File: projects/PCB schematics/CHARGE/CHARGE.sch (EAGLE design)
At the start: 30 parts, among them IC2 78L08SMD, Q1 IRLZ44Z, Q2 IRLZ44Z

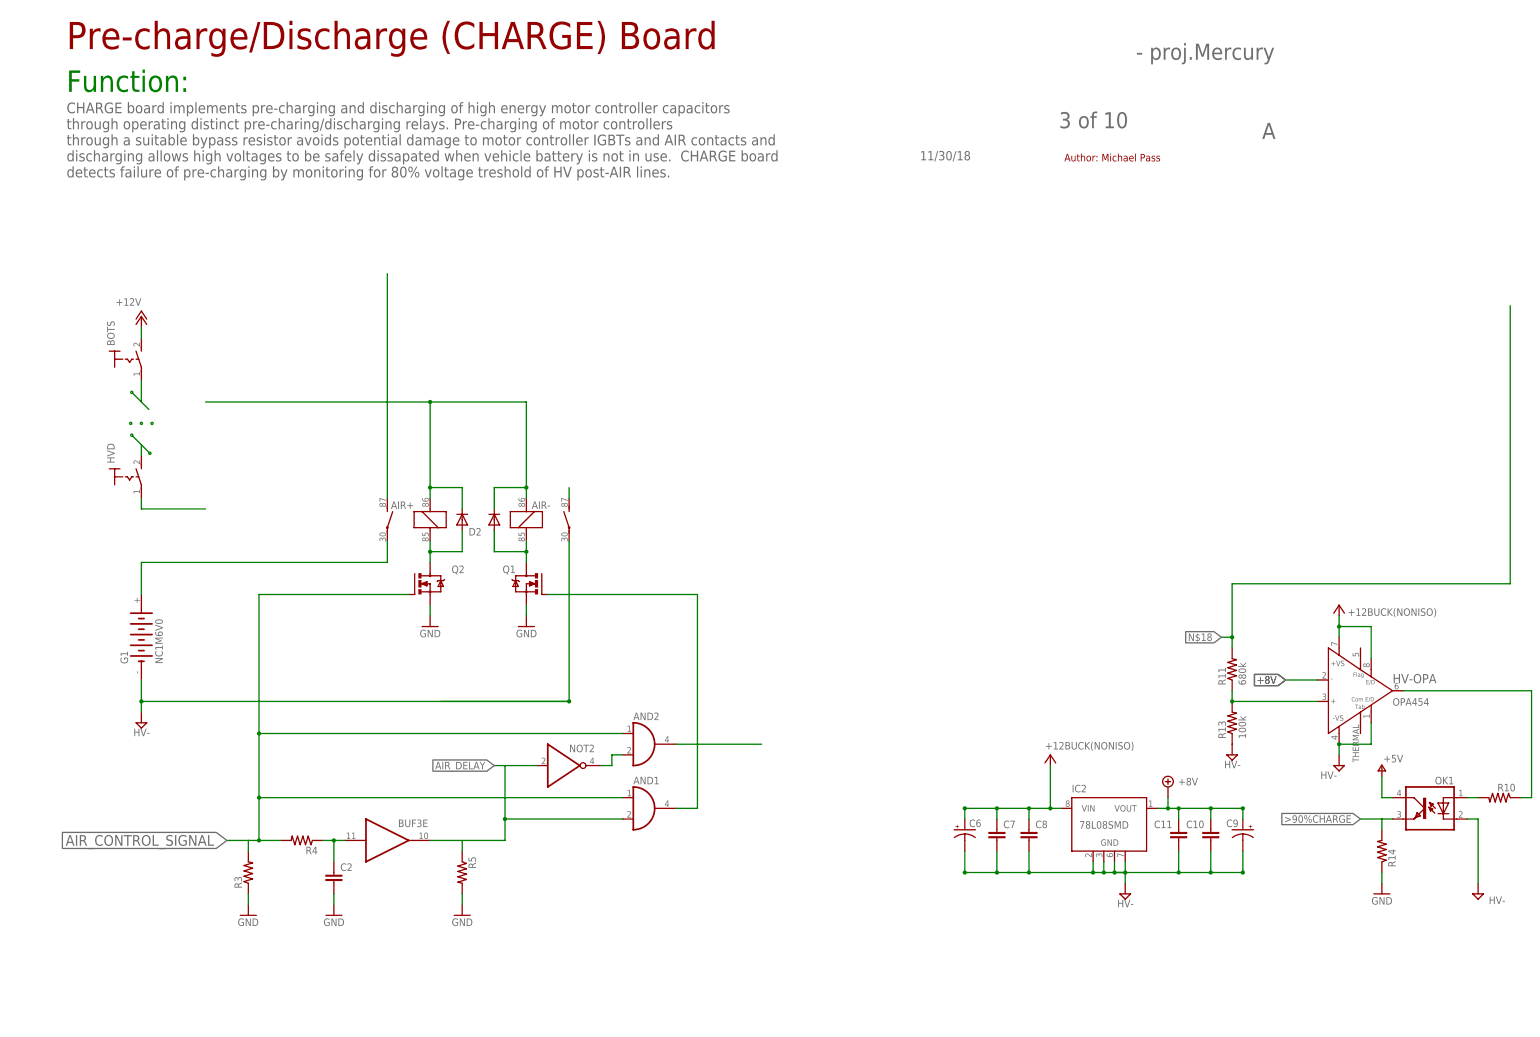
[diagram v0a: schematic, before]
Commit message: PROJ - Pulling in changes from mmp-CHARGE for ZEVA pre-charge
A library part was needed for ZEVA smart precharger  in order to play around with board placement. Very close approximation for footprint, with exact drill hole location achieved.

Amend - Incorrect stash attempt. Files copies over manually
from working mmp-CHARGE.
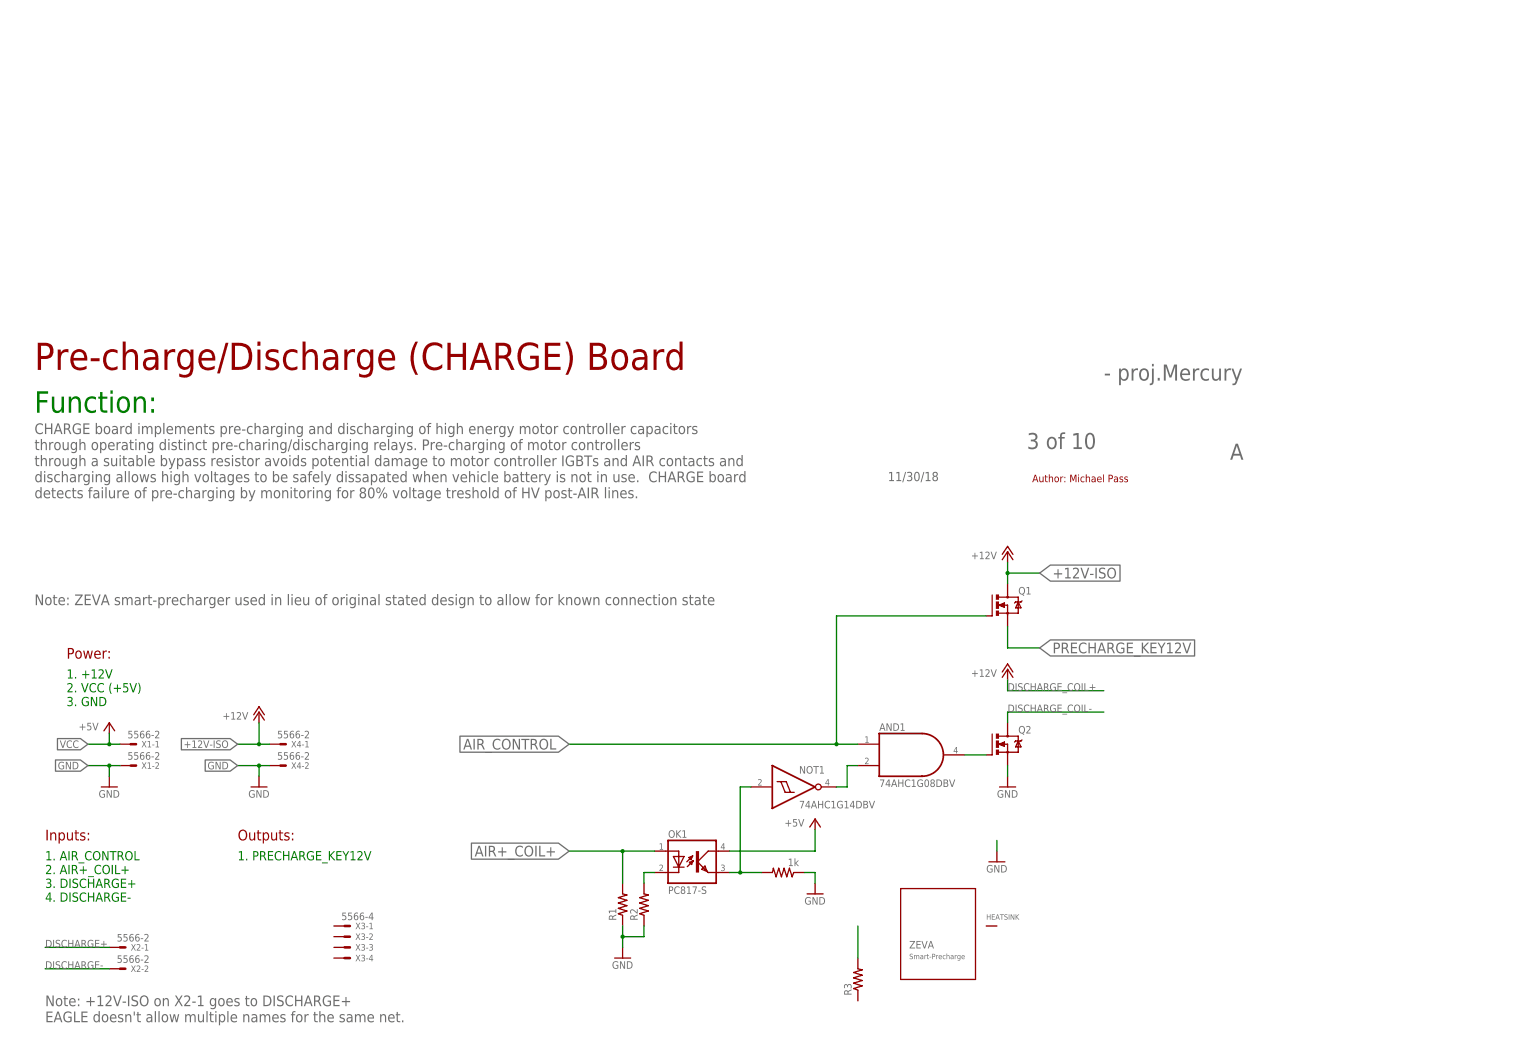
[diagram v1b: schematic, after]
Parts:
- removed AIR+, AIR-: CB1A-P-12V, relay:CB1A-P-12V
- removed AND2: 74AHCT1G08DCK, 74xx-little-de:74AHCT1G08DCK
- removed BOTS, HVD: (no value), switch:MS243
- removed BUF3: 7407D, 74xx-eu:7407D
- removed C10, C11, C7, C8: 0.1uF, rcl:C-EUC0805
- removed C2: (no value), rcl:C-EUC0805
- removed C6, C9: 10uF, rcl:CPOL-US085CS-1AW
- removed D1, D2: 1N4933, diode:1N4933
- removed G1: NC1M6V0, battery:NC1M6V0
- removed HV-OPA: OPA454, OPA454:OPA454
- removed IC2: 78L08SMD, linear:78L08SMD
- removed NOT2: 74LVC1G06DCK, 74xx-little-de:74LVC1G06DCK
- removed R10, R14, R4, R5: (no value), rcl:R-US_R0805
- removed R11: 680k, rcl:R-US_R0805
- removed R13: 100k, rcl:R-US_R0805
- added NOT1: 74AHC1G14DBV, 74xx-little-us:74AHC1G14DBV
- added R1, R2: (no value), rcl:R-US_R0805
- added R157: 1k, rcl:R-US_R0805
- added U$1: ZEVA_SMART-PRECHARGE, IowaFormula:ZEVA_SMART-PRECHARGE
- added X1, X2, X4: 5566-2, con-molex:5566-2
- added X3: 5566-4, con-molex:5566-4
- AND1: value 74AHCT1G08DCK -> 74AHC1G08DBV; device 74xx-little-de:74AHCT1G08DCK -> 74xx-little-us:74AHC1G08DBV
- OK1: device iowaFormula:PC817-S -> IowaFormula:PC817-S
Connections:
- removed net +12V: BOTS.S
- removed net +8V: C10.1, C11.1, C9.+, HV-OPA.IN-, IC2G$1.VOUT
- removed net >90%CHARGE: OK1.EMIT, R14.2
- removed net AIR_CONTROL_SIGNAL: AND1A.I0, AND2A.I0, Q2.G, R3.2, R4.2
- removed net AIR_DELAY: AND1A.I1, BUF3E.O, NOT2G$1.I, R5.1
- removed net HV+: AIR+2.P, G1.+
- removed net HV-: C10.2, C11.2, C6.-, C7.2, C8.2, C9.-, HV-OPA.-VS, HV-OPA.E/DCOM, IC2G$1.GND@1, IC2G$1.GND@2, IC2G$1.GND@3, IC2G$1.GND@4
- removed net HV-_CONTROL: AND1A.O, Q1.G
- removed net N$12: BOTS.P
- removed net N$13: HVD.S
- removed net N$14: AIR+1.1, AIR-1.1, D1.C, D2.C
- removed net N$17: OK1.A, R10.2
- removed net N$18: R11.2
- removed net N$20: BUF3E.I, C2.1, R4.1
- removed net N$21: AND2A.I1, NOT2G$1.O
- removed net N$27: AIR+2.S
- removed net N$31: AIR-2.S
- removed net N$7: AIR+1.2, D2.A, Q2.D
- removed net N$8: HV-OPA.OUT, R10.1
- removed net N$9: AIR-1.2, D1.A, Q1.D
- removed net V+: C6.+, C7.1, C8.1, HV-OPA.+VS, HV-OPA.E/D, IC2G$1.VIN, OK1.COL
- removed net VDIV_SIGNAL: HV-OPA.IN+, R11.1, R13.2
- new net +12V-ISO: Q1.D, X4-1.S
- new net AIR+_COIL+: OK1.A, R1.2
- new net AIR+_COIL+1: R3.2
- new net AIR_CONTROL: AND1A.I0, Q1.G
- new net DISCHARGE+: X2-1.S
- new net DISCHARGE-: X2-2.S
- new net DISCHARGE_COIL-: Q2.D
- new net OUTPUT77: NOT1A.I, OK1.EMIT, R157.2
- new net PRECHARGE_KEY12V: Q1.S
- new net TAB11: OK1.C, R2.2
- new net VCC: OK1.COL, X1-1.S
- net GND: now also R1.1, R157.1, R2.1, X1-2.S, X4-2.S; no longer AIR-2.P, C2.2, G1.-, OK1.C, Q1.S, R13.1, R14.1, R3.1, R5.2
- net N$1: now also AND1A.I1, NOT1A.O; no longer HVD.P
- net N$2: now also AND1A.O, Q2.G; no longer AND2A.O
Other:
- note added: "1. +12V 2. VCC (+5V) 3. GND"
- note added: "1. AIR_CONTROL 2. AIR+_COIL+ 3. DISCHARGE+ 4. DISCHARGE-"
- note added: "1. PRECHARGE_KEY12V"
- note added: "Inputs:"
- note added: "Note: +12V-ISO on X2-1 goes to DISCHARGE+ EAGLE doesn't allow multiple names for the same net."
- note added: "Note: ZEVA smart-precharger used in lieu of original stated design to allow for known connection state"
- note added: "Outputs:"
- note added: "Power:"
- moved on the sheet: OK1, Q1, Q2, R3

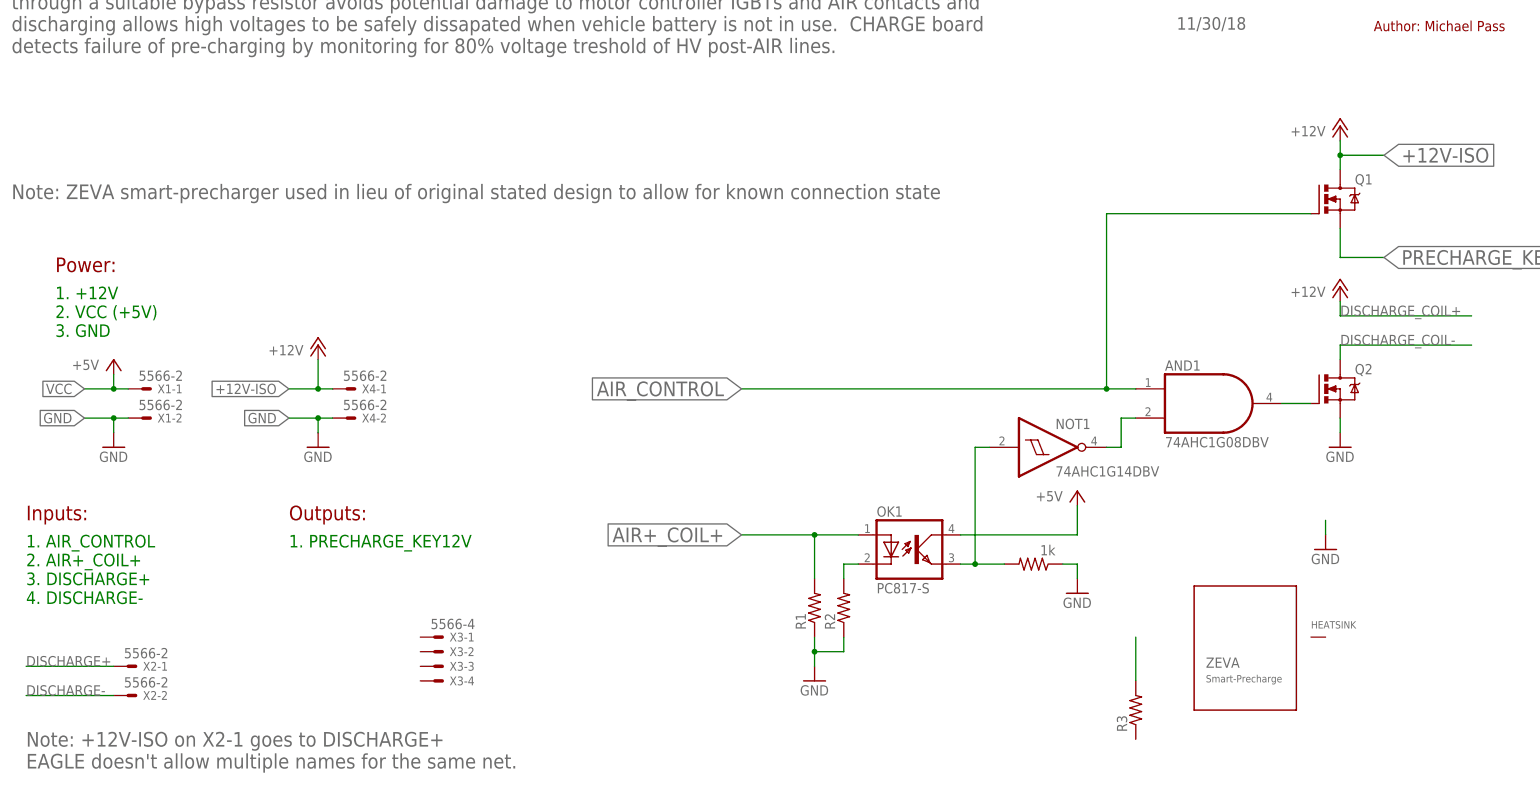
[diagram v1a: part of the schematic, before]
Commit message: CHARGE - Initial component placement/schematic revision.
A major design decision at this point will be whether or not to mount
the precharger onto the CHARGE board itself.

To determine this, schematic was revised, and parts were created to
test out footprint.

---SQUASH---

CHARGE - Checkout master to add ZEVA library.

ZEVA party created while in CHARGE branch.
Housekeeping down to merge this part into the master branch to make
it available to everyone.

---SQUASH---

SQUASH; CHARGE - Rebase with master

CHARGE - Routing code corruption.

---SQUASH---

CHARGE - Pull request revisions.

Final details finished for formal pull request. Revision requested.
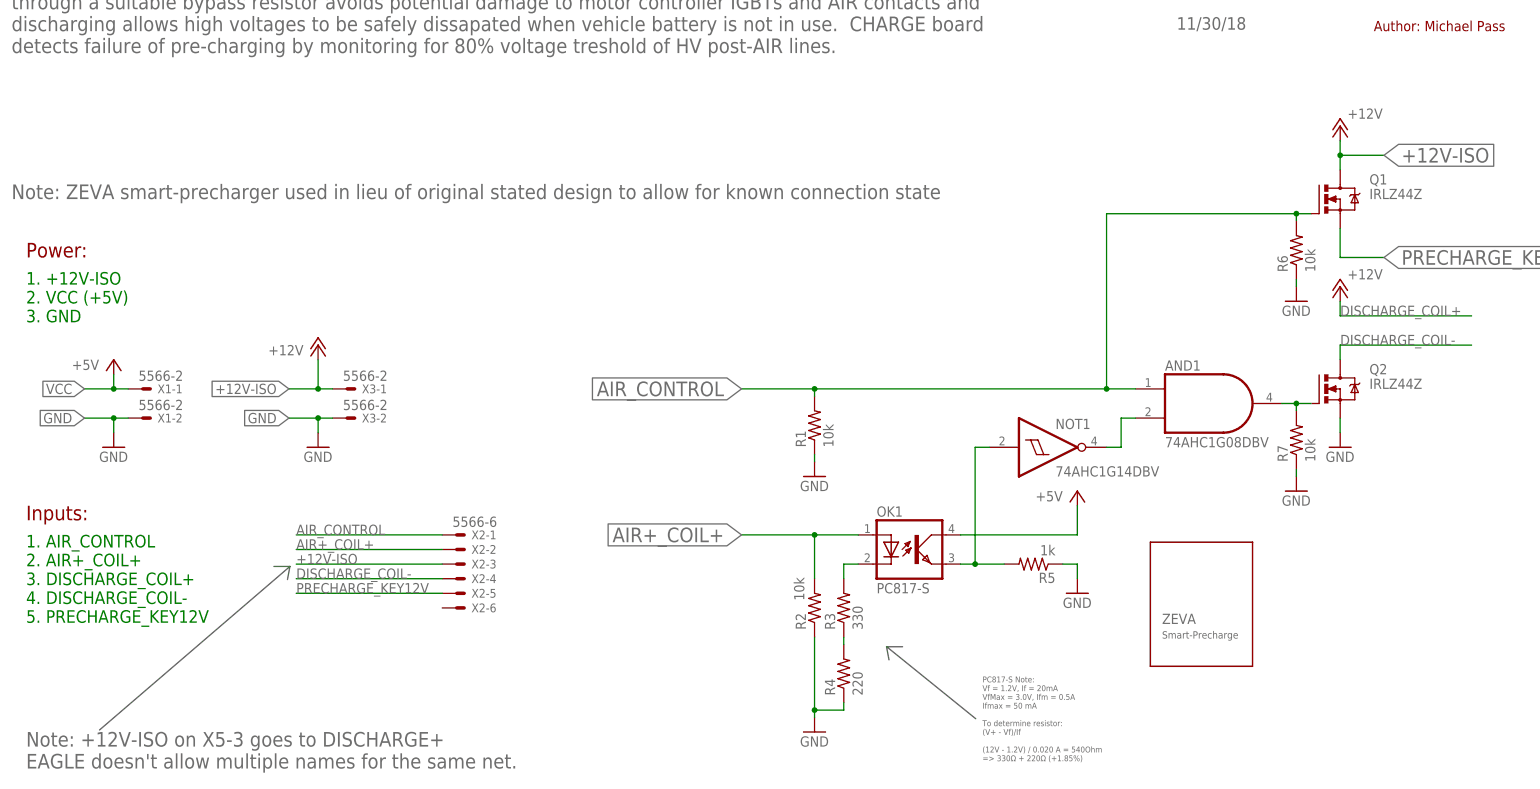
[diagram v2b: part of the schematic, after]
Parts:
- removed X4: 5566-2, con-molex:5566-2
- added R4: 220, rcl:R-US_R0805
- added R6, R7: 10k, rcl:R-US_R0805
- R1, R2: value (none) -> 10k
- R3: value (none) -> 330
- X2: value 5566-2 -> 5566-6; device con-molex:5566-2 -> con-molex:5566-6
- X3: value 5566-4 -> 5566-2; device con-molex:5566-4 -> con-molex:5566-2
- renumbered R157 to R5
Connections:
- net N$1 renamed NO_PRECHRG
- removed net AIR+_COIL+1: R3.2
- removed net DISCHARGE+: X2-1.S
- removed net DISCHARGE-: X2-2.S
- removed net N$2: AND1A.O, Q2.G
- new net DISCHARGE_MOSFET: AND1A.O, Q2.G, R7.2
- new net N$3: R3.1, R4.2
- net +12V-ISO: now also X2-3.S, X3-1.S; no longer X4-1.S
- net AIR+_COIL+: now also R2.2, X2-2.S; no longer R1.2
- net AIR_CONTROL: now also R1.2, R6.2, X2-1.S
- net DISCHARGE_COIL-: now also X2-4.S
- net GND: now also R4.1, R6.1, R7.1, X3-2.S; no longer X4-2.S
- net PRECHARGE_KEY12V: now also X2-5.S
- net TAB11: now also R3.2; no longer R2.2
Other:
- note added: "1. +12V-ISO 2. VCC (+5V) 3. GND"
- note added: "1. AIR_CONTROL 2. AIR+_COIL+ 3. DISCHARGE_COIL+ 4. DISCHARGE_COIL- 5. PRECHARGE_KEY12V"
- note added: "Note: +12V-ISO on X5-3 goes to DISCHARGE+ EAGLE doesn't allow multiple names for the same net."
- note added: "PC817-S Note: Vf = 1.2V, If = 20mA VfMax = 3.0V, Ifm = 0.5A Ifmax = 50 mA To determine resistor: (V+ - Vf)/If (12V - 1.2V) / 0.020 A = 540Ohm => 330Ω + 220Ω (+1.85%)"
- note removed: "1. +12V 2. VCC (+5V) 3. GND"
- note removed: "1. AIR_CONTROL 2. AIR+_COIL+ 3. DISCHARGE+ 4. DISCHARGE-"
- note removed: "1. PRECHARGE_KEY12V"
- note removed: "Note: +12V-ISO on X2-1 goes to DISCHARGE+ EAGLE doesn't allow multiple names for the same net."
- note removed: "Outputs:"
- moved on the sheet: R1, R2, R3, X2-1, X2-2, X3-1, X3-2
